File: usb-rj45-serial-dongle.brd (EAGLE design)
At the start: 34 x 19.8 mm, 16 parts, among them IC1 MAX202ECWE, J1 RJHSE-5381, J2 USBPCB_NOPASTE, U1 CP2102N-A01-GQFN20R, U2 SP0503BAHTG

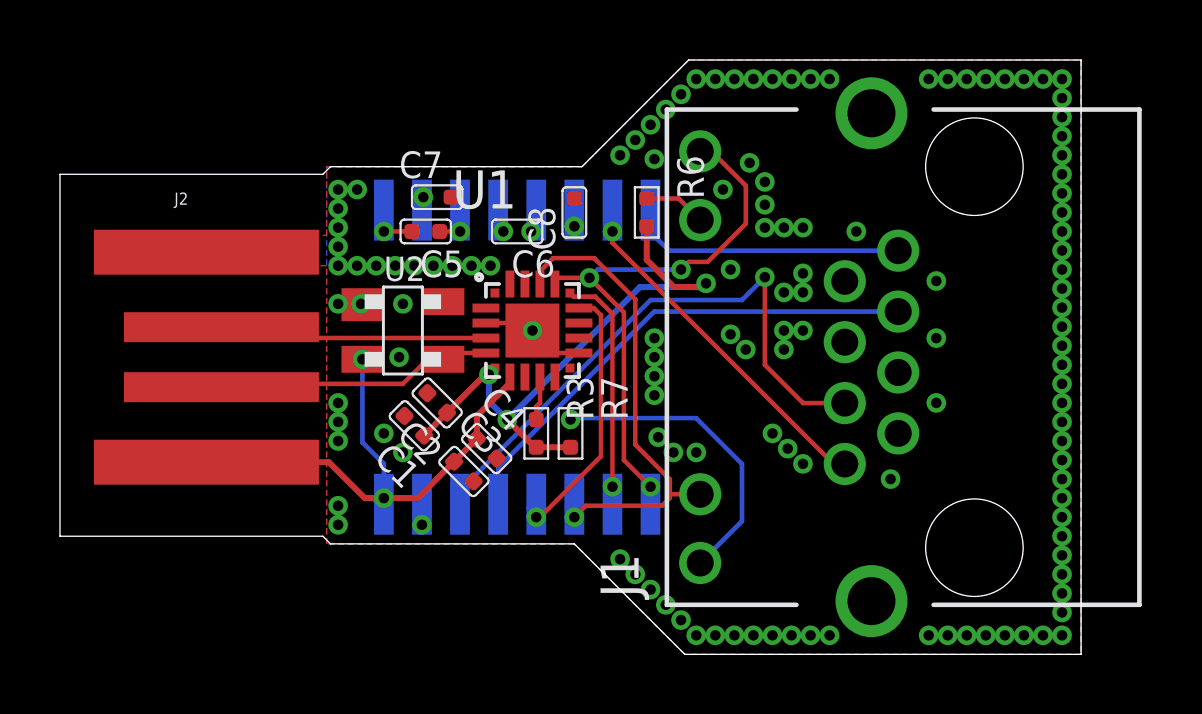
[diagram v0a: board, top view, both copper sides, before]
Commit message: Board updates, silkscreen cleanup and component changes
Board updates:
- GND plane stitching changed to a more general pattern rather than closely stitched to signal lines, since we aren't doing RF
- GND plane optimizations (bottom layer no longer separated into 2 distinct planes)
- Reduced size of board

Silkscreen cleanup:
- Removed values
- Rotated names and changed size/font to fit better and avoid vias (Seeed Fusion doesn't do blind via silkscreen well)

Component Changes:
- J1: RJHSE-5381 (shielded RJ45) replaced with RJHSE-5081 (unshielded RJ45) for smaller footprint and lower cost
- R3: Changed from Seeed OPL 0402 1KΩ 1% to 5% tolerance part due to value error (0R) on the 1% part
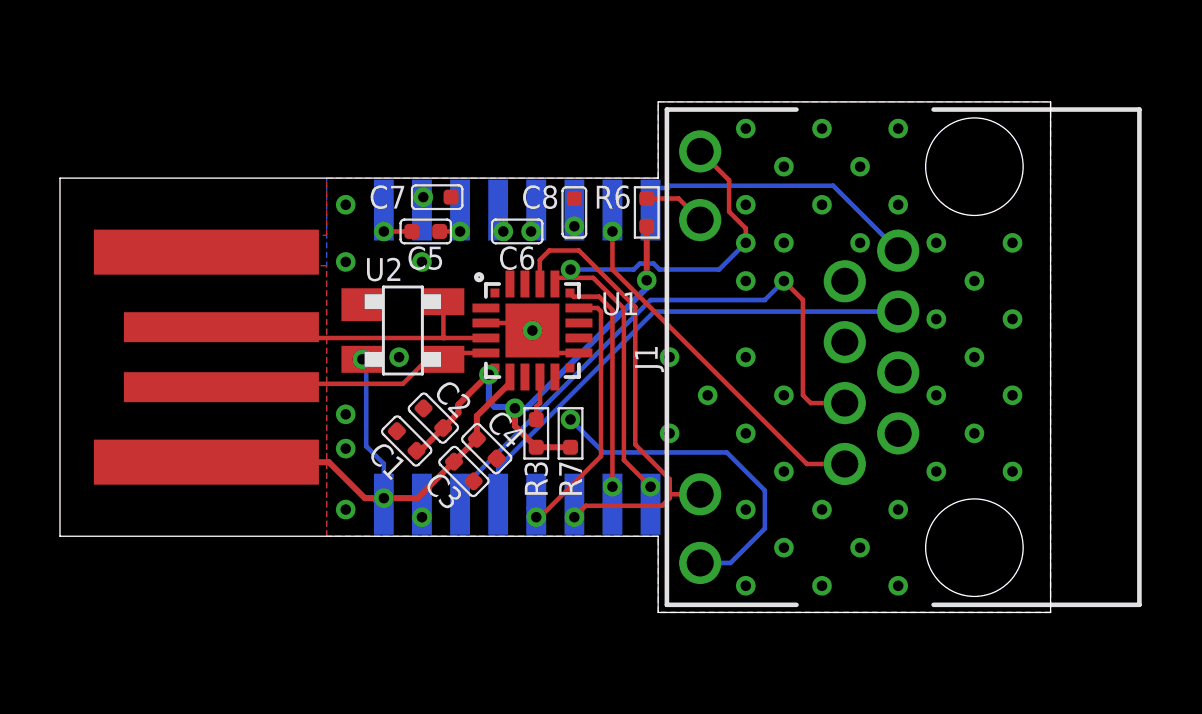
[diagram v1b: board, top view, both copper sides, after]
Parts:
- J1: value RJHSE-5381 -> RJHSE-5081; device RJHSE-5381:AMPHENOL_RJHSE-5381 -> RJHSE-5081:RJHSE-5081
- R3: value 0R -> 1K
- moved C1 0.57 mm to (11.6, 6.10)
- moved C2 0.52 mm to (12.4, 6.86)
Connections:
- net GND: no longer J1.S1, J1.S2
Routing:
- net 3V3: track 19.8 -> 16.6 mm
- net CTS: track 8.49 -> 9.96 mm
- net USBDP: track 8.97 -> 10.2 mm
- net N$3: track 10.2 -> 11.4 mm
- net UART_RXD: track 19.5 -> 20.2 mm
- net RTS: track 11.9 -> 12.4 mm
- net GND: vias 129 -> 46
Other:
- board size 34 x 19.8 mm -> 33 x 17 mm

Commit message: Renumber resistors to start from R1
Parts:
- removed R7: 330R, OPL_Resistor:R0402
- added R1: 1K, OPL_Resistor:R0402
- R3: value 1K -> 330R
- moved R3 1.14 mm to (17.0, 6.35)
- renumbered R6 to R2
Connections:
- net 3V3: now also R1.1; no longer R7.1
- net N$2: now also R1.2; no longer R3.2
- net N$3: now also R3.2; no longer R7.2
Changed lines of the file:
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@@
 </element>
 <element name="J2" library="SparkFun-Connectors" package="USB-A-PCB-NOPASTE" value="USBPCB_NOPASTE" x="5.08" y="8.89" smashed="yes"/>
-<element name="R3" library="OPL_Resistor" library_urn="urn:adsk.eagle:library:8004883" package="R0402" package3d_urn="urn:adsk.eagle:package:8004940/1" value="1K" x="15.875" y="6.35" smashed="yes" rot="R180">
+<element name="R1" library="OPL_Resistor" library_urn="urn:adsk.eagle:library:8004883" package="R0402" package3d_urn="urn:adsk.eagle:package:8004940/1" value="1K" x="15.875" y="6.35" smashed="yes" rot="R180">
 <attribute name="MPN" value="RC0402JR-071KL" x="-9.525" y="46.98999375" size="1.778" layer="27" rot="R180" display="off"/>
 <attribute name="NAME" x="15.87500625" y="5.461003125" size="0.762" layer="25" ratio="11" rot="R270" align="center-left"/>
 </element>
-<element name="R6" library="OPL_Resistor" library_urn="urn:adsk.eagle:library:8004883" package="R0402" package3d_urn="urn:adsk.eagle:package:8004940/1" value="330R" x="19.558" y="13.716" smashed="yes" rot="R180">
+<element name="R2" library="OPL_Resistor" library_urn="urn:adsk.eagle:library:8004883" package="R0402" package3d_urn="urn:adsk.eagle:package:8004940/1" value="330R" x="19.558" y="13.716" smashed="yes" rot="R180">
 <attribute name="MPN" value="RC0402FR-07330RL" x="-21.08199375" y="54.356" size="1.778" layer="27" rot="R180" display="off"/>
 <attribute name="NAME" x="19.05" y="14.223996875" size="0.762" layer="25" ratio="11" rot="R180" align="center-left"/>
 </element>
-<element name="R7" library="OPL_Resistor" library_urn="urn:adsk.eagle:library:8004883" package="R0402" package3d_urn="urn:adsk.eagle:package:8004940/1" value="330R" x="17.018" y="6.35" smashed="yes" rot="R180">
+<element name="R3" library="OPL_Resistor" library_urn="urn:adsk.eagle:library:8004883" package="R0402" package3d_urn="urn:adsk.eagle:package:8004940/1" value="330R" x="17.018" y="6.35" smashed="yes" rot="R180">
 <attribute name="MPN" value="RC0402FR-07330RL" x="-28.702" y="46.99" size="1.778" layer="27" rot="R180" display="off"/>
 <attribute name="NAME" x="17.018" y="5.461" size="0.762" layer="25" ratio="11" rot="R270" align="center-left"/>
@@
 <contactref element="C1" pad="1"/>
 <contactref element="C2" pad="1"/>
+<contactref element="R1" pad="1"/>
 <contactref element="R3" pad="1"/>
-<contactref element="R7" pad="1"/>
-<contactref element="R6" pad="1"/>
+<contactref element="R2" pad="1"/>
 <via x="15.164346875" y="7.187653125" extent="1-16" drill="0.35"/>
 <wire x1="14.4875375" y1="7.229465625" x2="14.297034375" y2="7.41996875" width="0.2032" layer="16"/>
@@
 <signal name="N$2">
 <contactref element="U1" pad="9"/>
-<contactref element="R3" pad="2"/>
+<contactref element="R1" pad="2"/>
 <wire x1="15.875" y1="6.8125" x2="15.875" y2="7.239" width="0.1524" layer="1"/>
 <wire x1="15.875" y1="7.239" x2="16.002" y2="7.366" width="0.1524" layer="1"/>
@@
 </signal>
 <signal name="N$3">
-<contactref element="R7" pad="2"/>
+<contactref element="R3" pad="2"/>
 <contactref element="J1" pad="12"/>
 <via x="17.018" y="6.8125" extent="1-16" drill="0.35"/>
@@
 </signal>
 <signal name="N$5">
-<contactref element="R6" pad="2"/>
+<contactref element="R2" pad="2"/>
 <contactref element="J1" pad="10"/>
 <wire x1="19.558" y1="14.1785" x2="20.6215" y2="14.1785" width="0.1524" layer="1"/>

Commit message: Renumber IC1 and other ICs to be in sequence with prefix "U"
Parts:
- removed IC1: MAX202ECWE, maxim:SO16L
- added U3: SP0503BAHTG, littlefuse:SOT143
- U2: value SP0503BAHTG -> MAX202ECWE; device littlefuse:SOT143 -> maxim:SO16L
- moved U2 3.91 mm to (15.2, 8.89), flipped to the bottom, turned to 180 degrees
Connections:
- net CTS: now also U2.8; no longer IC1.8
- net GND: now also U2.15, U3.1; no longer IC1.15, U2.1
- net N$1: now also U2.1; no longer IC1.1
- net N$4: now also U2.4; no longer IC1.4
- net N$6: now also U2.3; no longer IC1.3
- net N$7: now also U2.5; no longer IC1.5
- net N$8: now also U2.2; no longer IC1.2
- net N$9: now also U2.6; no longer IC1.6
- net RTS: now also U2.7; no longer IC1.7
- net RXD: now also U2.13; no longer IC1.13
- net TXD: now also U2.14; no longer IC1.14
- net UART_CTS: now also U2.12; no longer IC1.12
- net UART_RTS: now also U2.10; no longer IC1.10
- net UART_RXD: now also U2.9; no longer IC1.9
- net UART_TXD: now also U2.11; no longer IC1.11
- net USBDN: now also U3.3; no longer U2.3
- net USBDP: now also U3.4; no longer U2.4
- net VCC: now also U2.16, U3.2; no longer IC1.16, U2.2
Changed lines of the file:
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@@
 <attribute name="PRICE" value="None" x="47.497996875" y="-16.891" size="1.778" layer="27" display="off"/>
 </element>
-<element name="IC1" library="maxim" library_urn="urn:adsk.eagle:library:269" package="SO16L" package3d_urn="urn:adsk.eagle:package:17518/2" value="MAX202ECWE" x="15.24" y="8.89" smashed="yes" rot="MR180">
+<element name="U2" library="maxim" library_urn="urn:adsk.eagle:library:269" package="SO16L" package3d_urn="urn:adsk.eagle:package:17518/2" value="MAX202ECWE" x="15.24" y="8.89" smashed="yes" rot="MR180">
 <attribute name="MF" value="" x="15.24" y="8.89" size="1.778" layer="28" rot="MR180" display="off"/>
 <attribute name="MPN" value="MAX202ECWE+T" x="15.24" y="8.89" size="1.778" layer="28" rot="MR180" display="off"/>
@@
 <attribute name="NAME" x="16.637" y="14.224" size="0.762" layer="25" ratio="11" rot="R180" align="center-left"/>
 </element>
-<element name="U2" library="littlefuse" package="SOT143" value="SP0503BAHTG" x="11.43" y="9.779" smashed="yes">
+<element name="U3" library="littlefuse" package="SOT143" value="SP0503BAHTG" x="11.43" y="9.779" smashed="yes">
 <attribute name="NAME" x="10.795" y="11.43" size="0.762" layer="25" ratio="12" align="bottom-center"/>
 </element>
@@
 <vertex x="19.939" y="2.921"/>
 </polygon>
-<contactref element="IC1" pad="15"/>
+<contactref element="U2" pad="15"/>
 <contactref element="C7" pad="2"/>
 <contactref element="C8" pad="2"/>
-<contactref element="U2" pad="1"/>
+<contactref element="U3" pad="1"/>
 <wire x1="14.198" y1="10.029" x2="15.498" y2="10.029" width="0.1524" layer="1"/>
 <wire x1="15.498" y1="10.029" x2="15.748" y2="9.779" width="0.1524" layer="1"/>
@@
 <signal name="RXD">
 <contactref element="J1" pad="3"/>
-<contactref element="IC1" pad="13"/>
+<contactref element="U2" pad="13"/>
 <wire x1="27.94" y1="10.41" x2="19.808" y2="10.41" width="0.1524" layer="16"/>
 <wire x1="19.808" y1="10.41" x2="14.605" y2="5.207" width="0.1524" layer="16"/>
@@
 <signal name="CTS">
 <contactref element="J1" pad="1"/>
-<contactref element="IC1" pad="8"/>
+<contactref element="U2" pad="8"/>
 <wire x1="27.94" y1="12.44" x2="25.775" y2="14.605" width="0.1524" layer="16"/>
 <wire x1="20.2692" y1="14.605" x2="20.2692" y2="14.5288" width="0.1524" layer="16"/>
@@
 <signal name="TXD">
 <contactref element="J1" pad="6"/>
-<contactref element="IC1" pad="14"/>
+<contactref element="U2" pad="14"/>
 <wire x1="13.335" y1="3.9878" x2="13.335" y2="4.445" width="0.1524" layer="16"/>
 <wire x1="13.335" y1="4.445" x2="19.685" y2="10.795" width="0.1524" layer="16"/>
@@
 <signal name="RTS">
 <contactref element="J1" pad="8"/>
-<contactref element="IC1" pad="7"/>
+<contactref element="U2" pad="7"/>
 <wire x1="26.16" y1="5.33" x2="24.896" y2="5.33" width="0.1524" layer="1"/>
 <wire x1="18.415" y1="11.811" x2="18.415" y2="13.081" width="0.1524" layer="1"/>
@@
 <contactref element="U1" pad="18"/>
 <contactref element="J1" pad="11"/>
-<contactref element="IC1" pad="11"/>
+<contactref element="U2" pad="11"/>
 <wire x1="15.9924" y1="12.1276875" x2="15.9924" y2="11.3346" width="0.1524" layer="1"/>
 <wire x1="15.998" y1="11.329" x2="15.9924" y2="11.3346" width="0.1524" layer="1"/>
@@
 <contactref element="U1" pad="17"/>
 <contactref element="J1" pad="9"/>
-<contactref element="IC1" pad="9"/>
+<contactref element="U2" pad="9"/>
 <wire x1="16.498" y1="11.329" x2="16.49799375" y2="11.5346" width="0.1524" layer="1"/>
 <wire x1="16.49799375" y1="11.5346" x2="17.018" y2="11.5346" width="0.1524" layer="1"/>
@@
 <signal name="UART_RTS">
 <contactref element="U1" pad="16"/>
-<contactref element="IC1" pad="10"/>
+<contactref element="U2" pad="10"/>
 <wire x1="17.97145625" y1="10.9076" x2="17.1194" y2="10.9076" width="0.1524" layer="1"/>
 <wire x1="16.998" y1="11.029" x2="17.1194" y2="10.9076" width="0.1524" layer="1"/>
@@
 <signal name="UART_CTS">
 <contactref element="U1" pad="15"/>
-<contactref element="IC1" pad="12"/>
+<contactref element="U2" pad="12"/>
 <wire x1="18.034" y1="5.588" x2="16.002" y2="3.556" width="0.1524" layer="1"/>
 <wire x1="16.002" y1="3.556" x2="15.875" y2="3.556" width="0.1524" layer="1"/>
@@
 <contactref element="U1" pad="4"/>
 <contactref element="J2" pad="USB_P"/>
-<contactref element="U2" pad="4"/>
+<contactref element="U3" pad="4"/>
 <wire x1="5.38" y1="9.89" x2="7.763" y2="9.89" width="0.1524" layer="1"/>
 <wire x1="14.198" y1="9.529" x2="12.827" y2="9.529" width="0.1524" layer="1"/>
@@
 <contactref element="U1" pad="5"/>
 <contactref element="J2" pad="USB_M"/>
-<contactref element="U2" pad="3"/>
+<contactref element="U3" pad="3"/>
 <wire x1="14.198" y1="9.029" x2="12.78" y2="9.029" width="0.1524" layer="1"/>
 <wire x1="12.78" y1="9.029" x2="12.78" y2="8.819" width="0.1524" layer="1"/>
@@
 </signal>
 <signal name="VCC">
-<contactref element="IC1" pad="16"/>
+<contactref element="U2" pad="16"/>
 <contactref element="C3" pad="1"/>
 <contactref element="C4" pad="1"/>
@@
 <wire x1="13.8969625" y1="6.931034375" x2="13.8969625" y2="6.169034375" width="0.2032" layer="1"/>
 <wire x1="13.8969625" y1="6.169034375" x2="13.1349625" y2="5.407034375" width="0.2032" layer="1"/>
-<contactref element="U2" pad="2"/>
+<contactref element="U3" pad="2"/>
 <via x="10.08" y="8.819" extent="1-16" drill="0.35"/>
 <wire x1="10.08" y1="8.819" x2="10.207" y2="8.692" width="0.1524" layer="16"/>
@@
 </signal>
 <signal name="N$1">
-<contactref element="IC1" pad="1"/>
+<contactref element="U2" pad="1"/>
 <contactref element="C5" pad="2"/>
 <wire x1="11.7295" y1="13.081" x2="10.795" y2="13.081" width="0.1524" layer="1"/>
@@
 </signal>
 <signal name="N$4">
-<contactref element="IC1" pad="4"/>
+<contactref element="U2" pad="4"/>
 <contactref element="C6" pad="2"/>
 <wire x1="14.605" y1="13.7922" x2="14.7775" y2="13.6197" width="0.1524" layer="16"/>
@@
 <signal name="N$6">
 <contactref element="C5" pad="1"/>
-<contactref element="IC1" pad="3"/>
+<contactref element="U2" pad="3"/>
 <wire x1="12.6545" y1="13.081" x2="13.335" y2="13.081" width="0.1524" layer="1"/>
 <via x="13.335" y="13.081" extent="1-16" drill="0.35"/>
@@
 <signal name="N$7">
 <contactref element="C6" pad="1"/>
-<contactref element="IC1" pad="5"/>
+<contactref element="U2" pad="5"/>
 <via x="15.7025" y="13.081" extent="1-16" drill="0.35"/>
 <wire x1="15.7025" y1="13.081" x2="15.875" y2="13.2535" width="0.1524" layer="16"/>
@@
 </signal>
 <signal name="N$8">
-<contactref element="IC1" pad="2"/>
+<contactref element="U2" pad="2"/>
 <contactref element="C7" pad="1"/>
 <via x="12.1105" y="14.224" extent="1-16" drill="0.35"/>
@@
 </signal>
 <signal name="N$9">
-<contactref element="IC1" pad="6"/>
+<contactref element="U2" pad="6"/>
 <contactref element="C8" pad="1"/>
 <via x="17.145" y="13.2535" extent="1-16" drill="0.35"/>

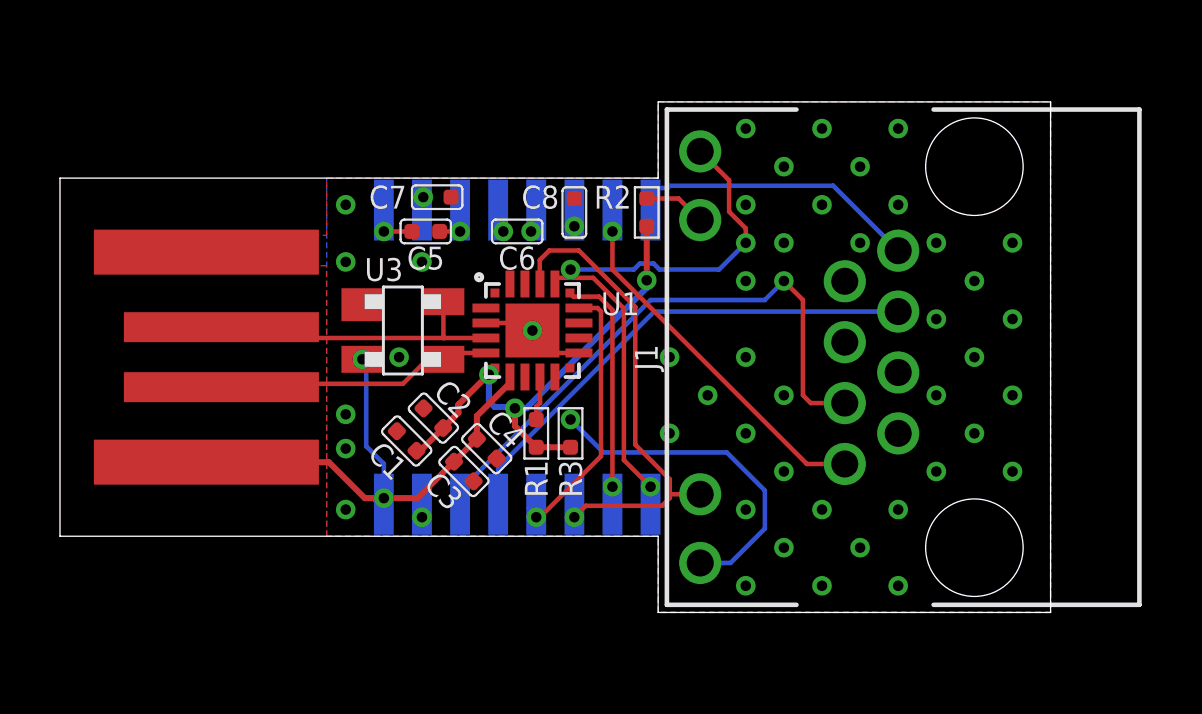
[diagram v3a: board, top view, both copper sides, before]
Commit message: Use CP2102 TXT/RXT pins to drive LEDs, thanks @MatsK for pointing this feature out
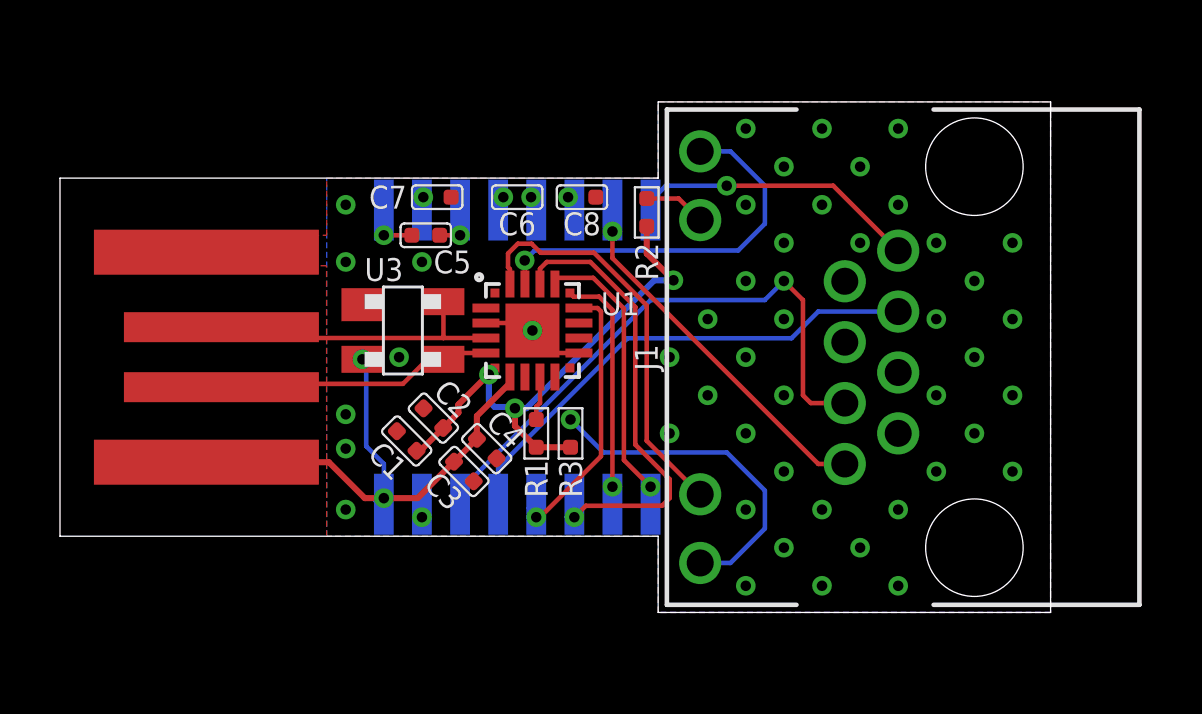
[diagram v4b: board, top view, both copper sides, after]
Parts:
- moved C6 1.14 mm to (15.2, 14.2)
- moved C8 0.57 mm to (17.4, 14.2), turned to 90 degrees
- moved C5 0.13 mm to (12.2, 13.0)
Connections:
- new net RXT_LED: J1.9, U1.19
- new net TXT_LED: J1.11, U1.20
- net UART_RXD: no longer J1.9
- net UART_TXD: no longer J1.11
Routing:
- net TXT_LED: track 0.00 -> 13.7 mm
- net RXT_LED: track 0.00 -> 13.2 mm, vias 0 -> 1
- net UART_RXD: track 20.2 -> 9.82 mm, vias 3 -> 1
- net UART_TXD: track 16.6 -> 15.1 mm
- net 3V3: track 16.6 -> 17.7 mm
- net CTS: track 9.96 -> 10.4 mm, vias 0 -> 1
- net GND: vias 46 -> 48
